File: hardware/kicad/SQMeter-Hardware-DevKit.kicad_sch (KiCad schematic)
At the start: 46 parts, among them J1 12V IN, J10 AUX, J11 DevKitC-1 J1, J12 DevKitC-1 J3, J3 I2C TSL2591, J4 I2C MLX90614, J5 I2C BME280, J6 I2C SPARE, J7 GPS, J8 RG-15, J9 WIND, Q1 AO3401A, U1 AP63205WU, U4 USBLC6-2SC6, U5 USBLC6-2SC6, U6 USBLC6-2SC6

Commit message: feat: Waveshare ESP32-S3-Zero socket variant and one GPIO map for all boards
- SQM_VARIANT=zero: ESP32-S3-Zero-M on 2x9 sockets (Waveshare pinout and
  drawing), same 5 V feed scheme as the DevKit variant
- GPIO map unified across module, DevKit and Zero (limited by the Zero's
  GPIO1-13 headers): RG-15 1/2, wind 4/5, I2C 8/9, GPS 12/13, AUX 6/7/10/11
- fab exports for all three
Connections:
- net GPS_RX: now also J11.19 (Pin_19); no longer J11.11 (Pin_11)
- net GPS_TX: now also J11.18 (Pin_18); no longer J11.10 (Pin_10)
- net RG_RX: now also J12.5 (Pin_5); no longer J11.9 (Pin_9)
- net RG_TX: now also J12.4 (Pin_4); no longer J11.8 (Pin_8)
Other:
- note added: "12 V input, protection, 5V buck to dev board"
- note removed: "12 V input, protection, 5V buck to DevKit"
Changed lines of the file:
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@@
   )
   (text
-    "12 V input, protection, 5V buck to DevKit"
+    "12 V input, protection, 5V buck to dev board"
     (exclude_from_sim no)
     (at 15.24 25.4 0)
@@
     (property
       "Description"
-      "Stops DevKit USB back-feeding the buck"
+      "Dev board USB can't back-feed the buck; buck can't push into a PC"
       (at 109.22 76.2 0)
       (effects
@@
     )
   )
-  (label
-    "RG_TX"
-    (at 31.75 203.2 180)
-    (effects
-      (font
-        (size 1.27 1.27)
-      )
-      (justify right bottom)
-    )
+  (no_connect
+    (at 31.75 203.2)
   )
-  (label
-    "RG_RX"
-    (at 31.75 205.74 180)
-    (effects
-      (font
-        (size 1.27 1.27)
-      )
-      (justify right bottom)
-    )
+  (no_connect
+    (at 31.75 205.74)
   )
-  (label
-    "GPS_TX"
-    (at 31.75 208.28 180)
-    (effects
-      (font
-        (size 1.27 1.27)
-      )
-      (justify right bottom)
-    )
+  (no_connect
+    (at 31.75 208.28)
   )
-  (label
-    "GPS_RX"
-    (at 31.75 210.82 180)
-    (effects
-      (font
-        (size 1.27 1.27)
-      )
-      (justify right bottom)
-    )
+  (no_connect
+    (at 31.75 210.82)
   )
   (label
@@
     )
   )
-  (no_connect
-    (at 31.75 228.6)
+  (label
+    "GPS_TX"
+    (at 31.75 228.6 180)
+    (effects
+      (font
+        (size 1.27 1.27)
+      )
+      (justify right bottom)
+    )
   )
-  (no_connect
-    (at 31.75 231.14)
+  (label
+    "GPS_RX"
+    (at 31.75 231.14 180)
+    (effects
+      (font
+        (size 1.27 1.27)
+      )
+      (justify right bottom)
+    )
   )
   (no_connect
@@
     (at 76.2 190.5)
   )
-  (no_connect
-    (at 76.2 193.04)
+  (label
+    "RG_TX"
+    (at 76.2 193.04 180)
+    (effects
+      (font
+        (size 1.27 1.27)
+      )
+      (justify right bottom)
+    )
   )
-  (no_connect
-    (at 76.2 195.58)
+  (label
+    "RG_RX"
+    (at 76.2 195.58 180)
+    (effects
+      (font
+        (size 1.27 1.27)
+      )
+      (justify right bottom)
+    )
   )
   (no_connect

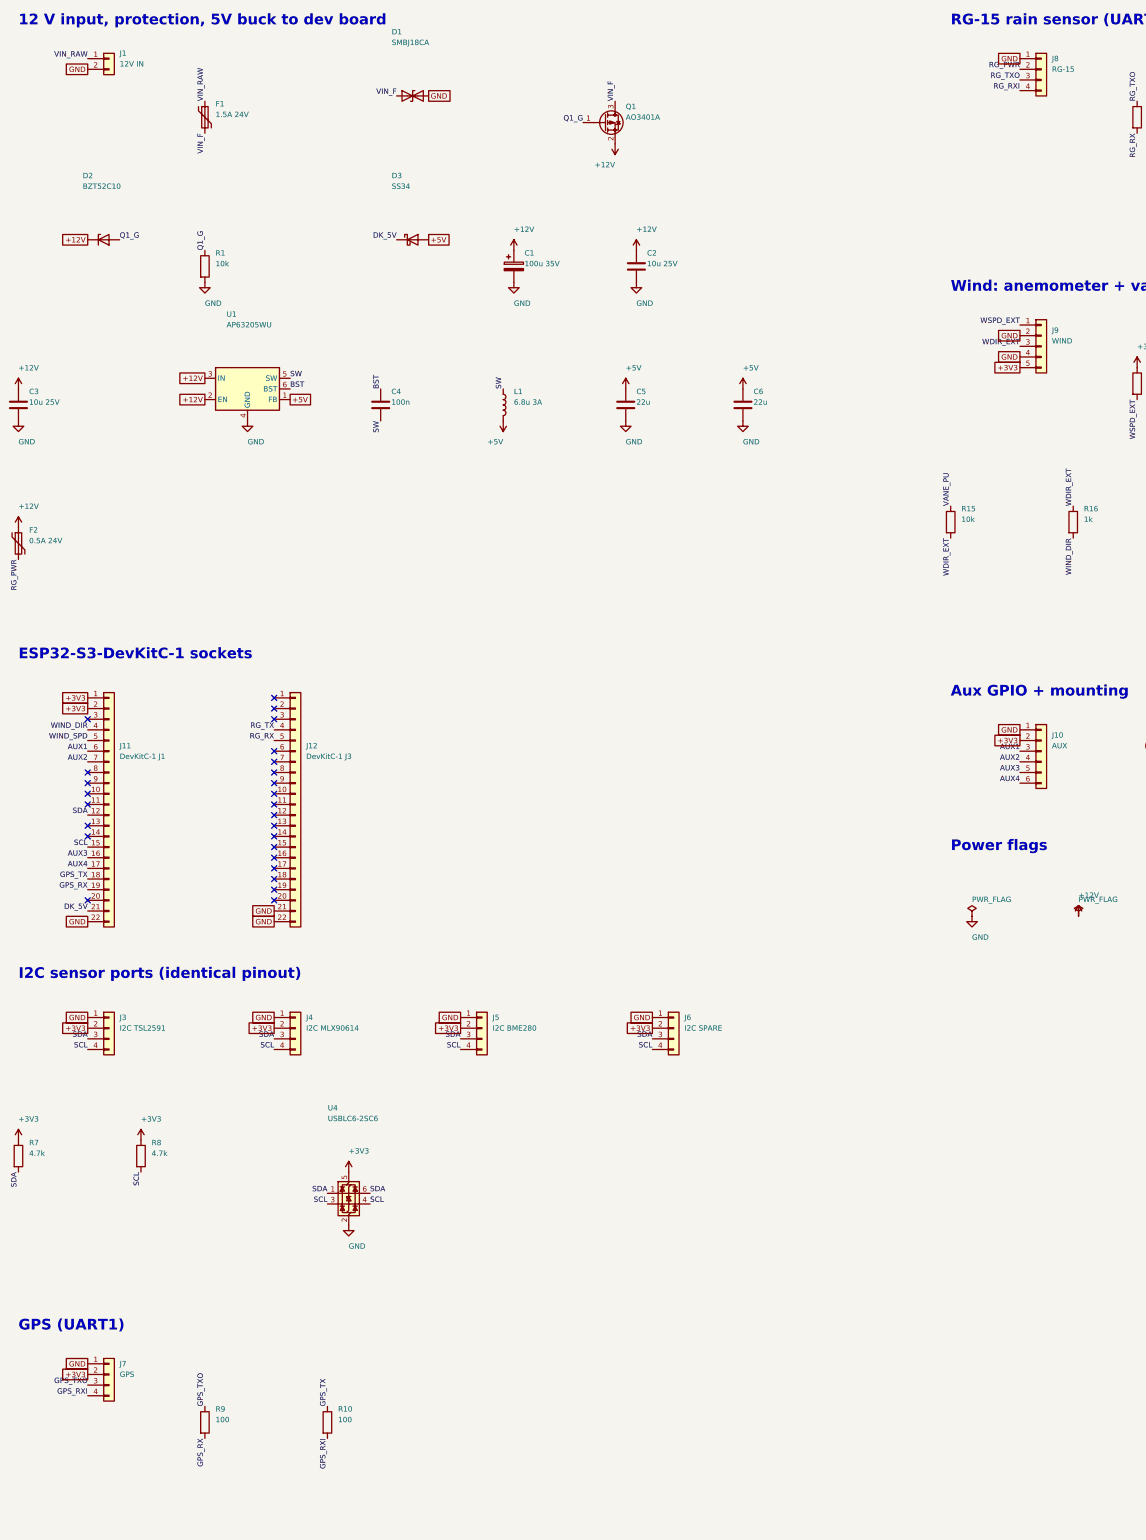
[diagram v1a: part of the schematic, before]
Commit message: feat: second I2C bus for a second TSL2591 (SQM + SQM-L)
TSL2591 has a fixed address, so the second sensor gets its own bus on
GPIO10/11 (I2C-2 JST-XH port, own pull-ups and ESD). AUX drops to IO6/IO7.
Q1 gate zener replaced by a resistor divider (one fewer extended part).
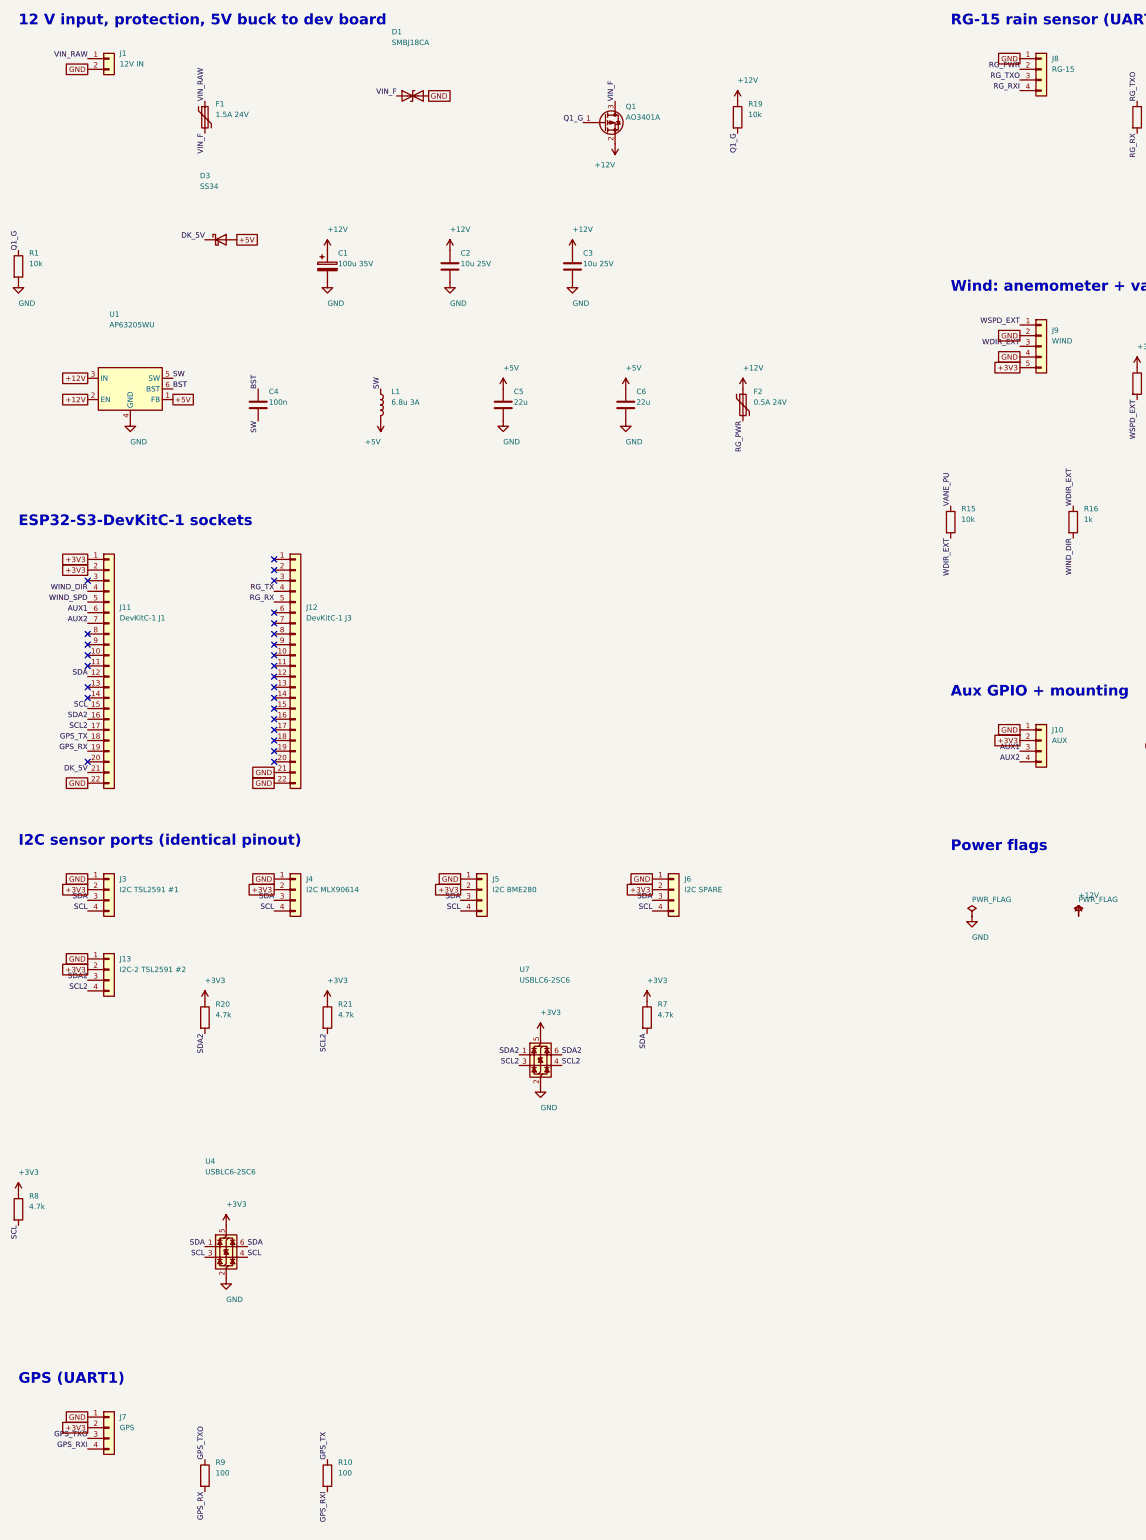
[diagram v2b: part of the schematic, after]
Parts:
- removed D2: BZT52C10, Diode_SMD:D_SOD-123, symbol Device:D_Zener
- removed J10: AUX, Connector_JST:JST_XH_B6B-XH-A_1x06_P2.50mm_Vertical, symbol Connector_Generic:Conn_01x06
- added J10: AUX, Connector_JST:JST_XH_B4B-XH-A_1x04_P2.50mm_Vertical, symbol Connector_Generic:Conn_01x04
- added J13: I2C-2 TSL2591 #2, Connector_JST:JST_XH_B4B-XH-A_1x04_P2.50mm_Vertical, symbol Connector_Generic:Conn_01x04
- added R19: 10k, Resistor_SMD:R_0603_1608Metric, symbol Device:R
- added R20, R21: 4.7k, Resistor_SMD:R_0603_1608Metric, symbol Device:R
- added U7: USBLC6-2SC6, Package_TO_SOT_SMD:SOT-23-6, symbol Power_Protection:USBLC6-2SC6
- J3: value I2C TSL2591 -> I2C TSL2591 #1
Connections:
- net +12V: now also R19.1
- net +3V3: now also J10.2 (Pin_2), J13.2 (Pin_2), R20.1, R21.1, U7.5 (VBUS)
- net AUX1: now also J10.3 (Pin_3)
- net AUX2: now also J10.4 (Pin_4)
- net GND: now also J10.1 (Pin_1), J13.1 (Pin_1), U7.2 (GND)
- net Q1_G: now also R19.2
- net AUX3 renamed SDA2
- net SDA2: now also J13.3 (Pin_3), R20.2, U7.1 (I/O1), U7.6 (I/O1)
- net AUX4 renamed SCL2
- net SCL2: now also J13.4 (Pin_4), R21.2, U7.3 (I/O2), U7.4 (I/O2)
